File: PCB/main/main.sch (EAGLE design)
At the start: 19 parts, among them T1 2SC1815

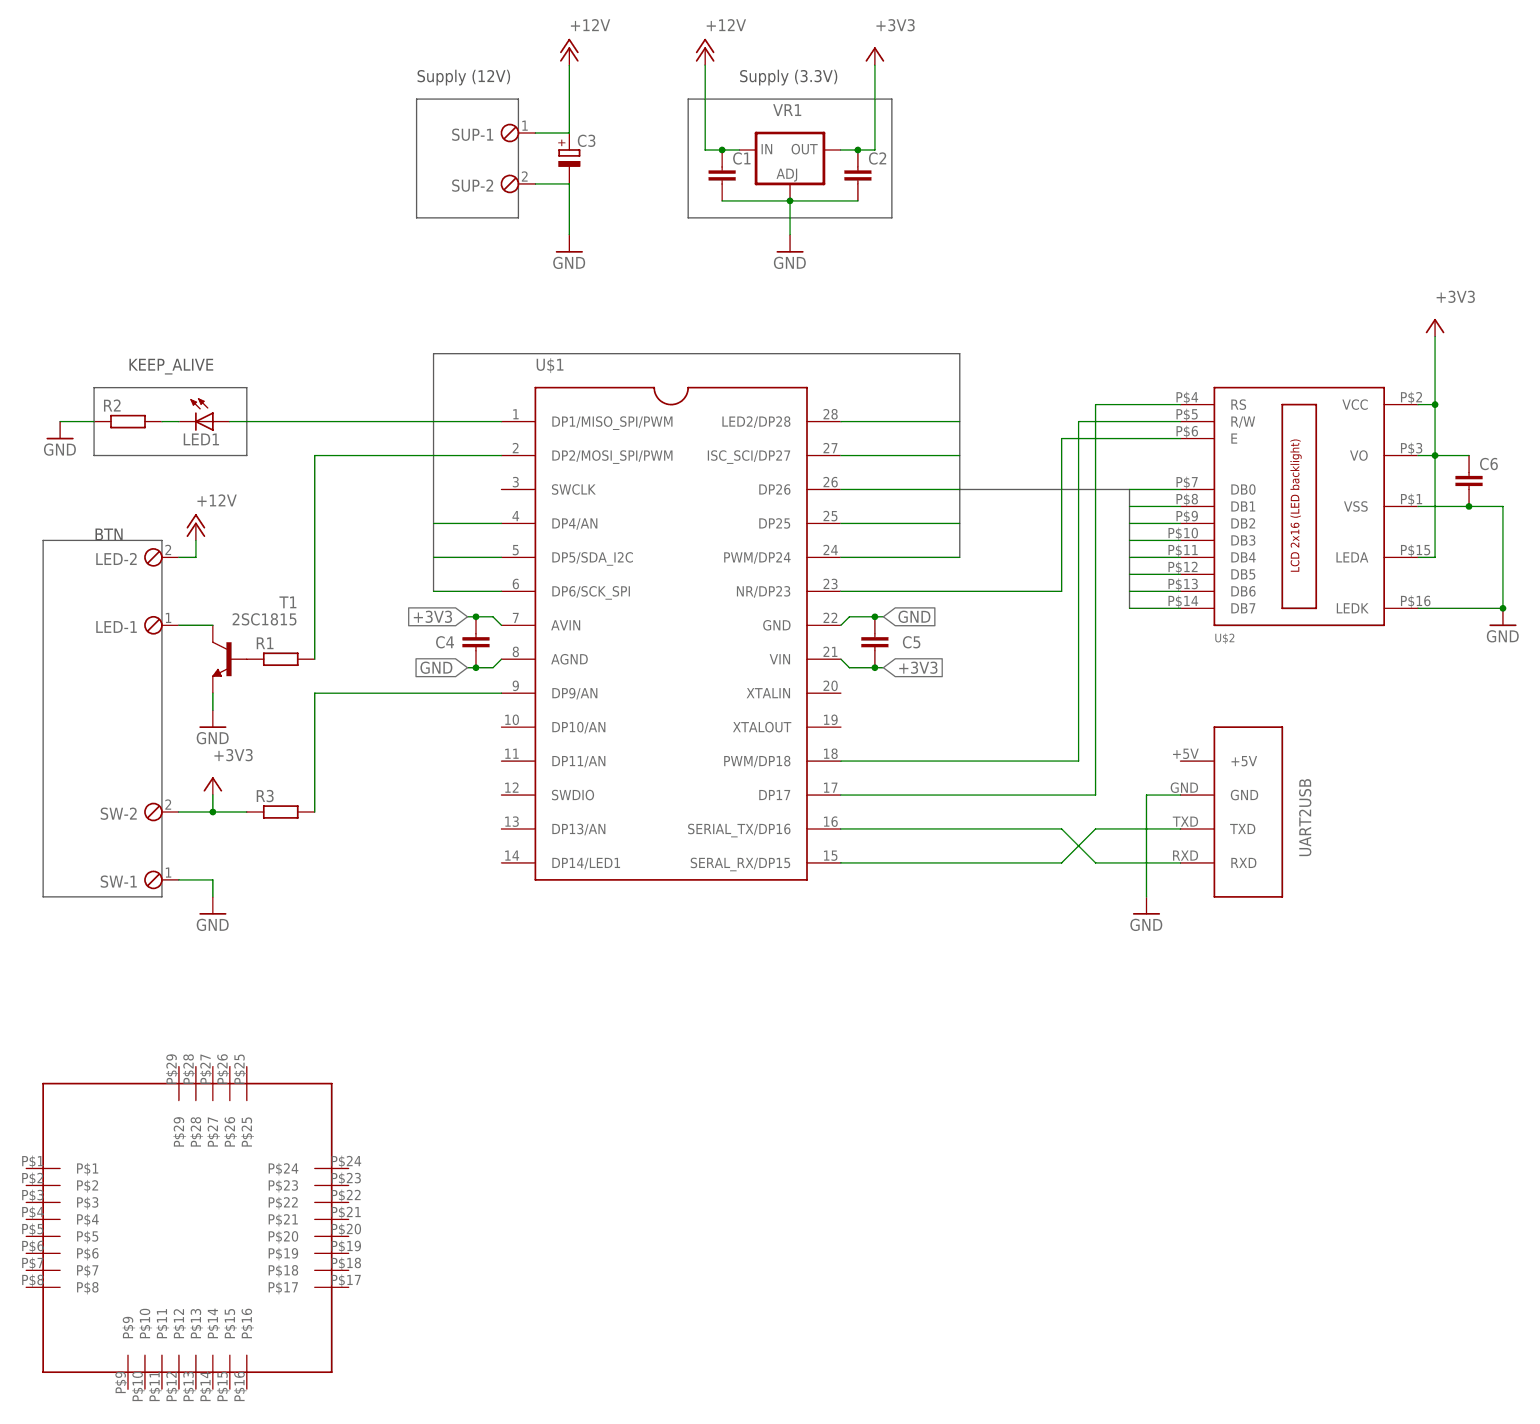
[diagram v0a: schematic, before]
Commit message: PCB: Add DIP con for programing writer like isp writer.
Note that the pin assignment was modified because "reset" and"ISP Enable"
pins are required by "ISP writer" but they were used for LCD.
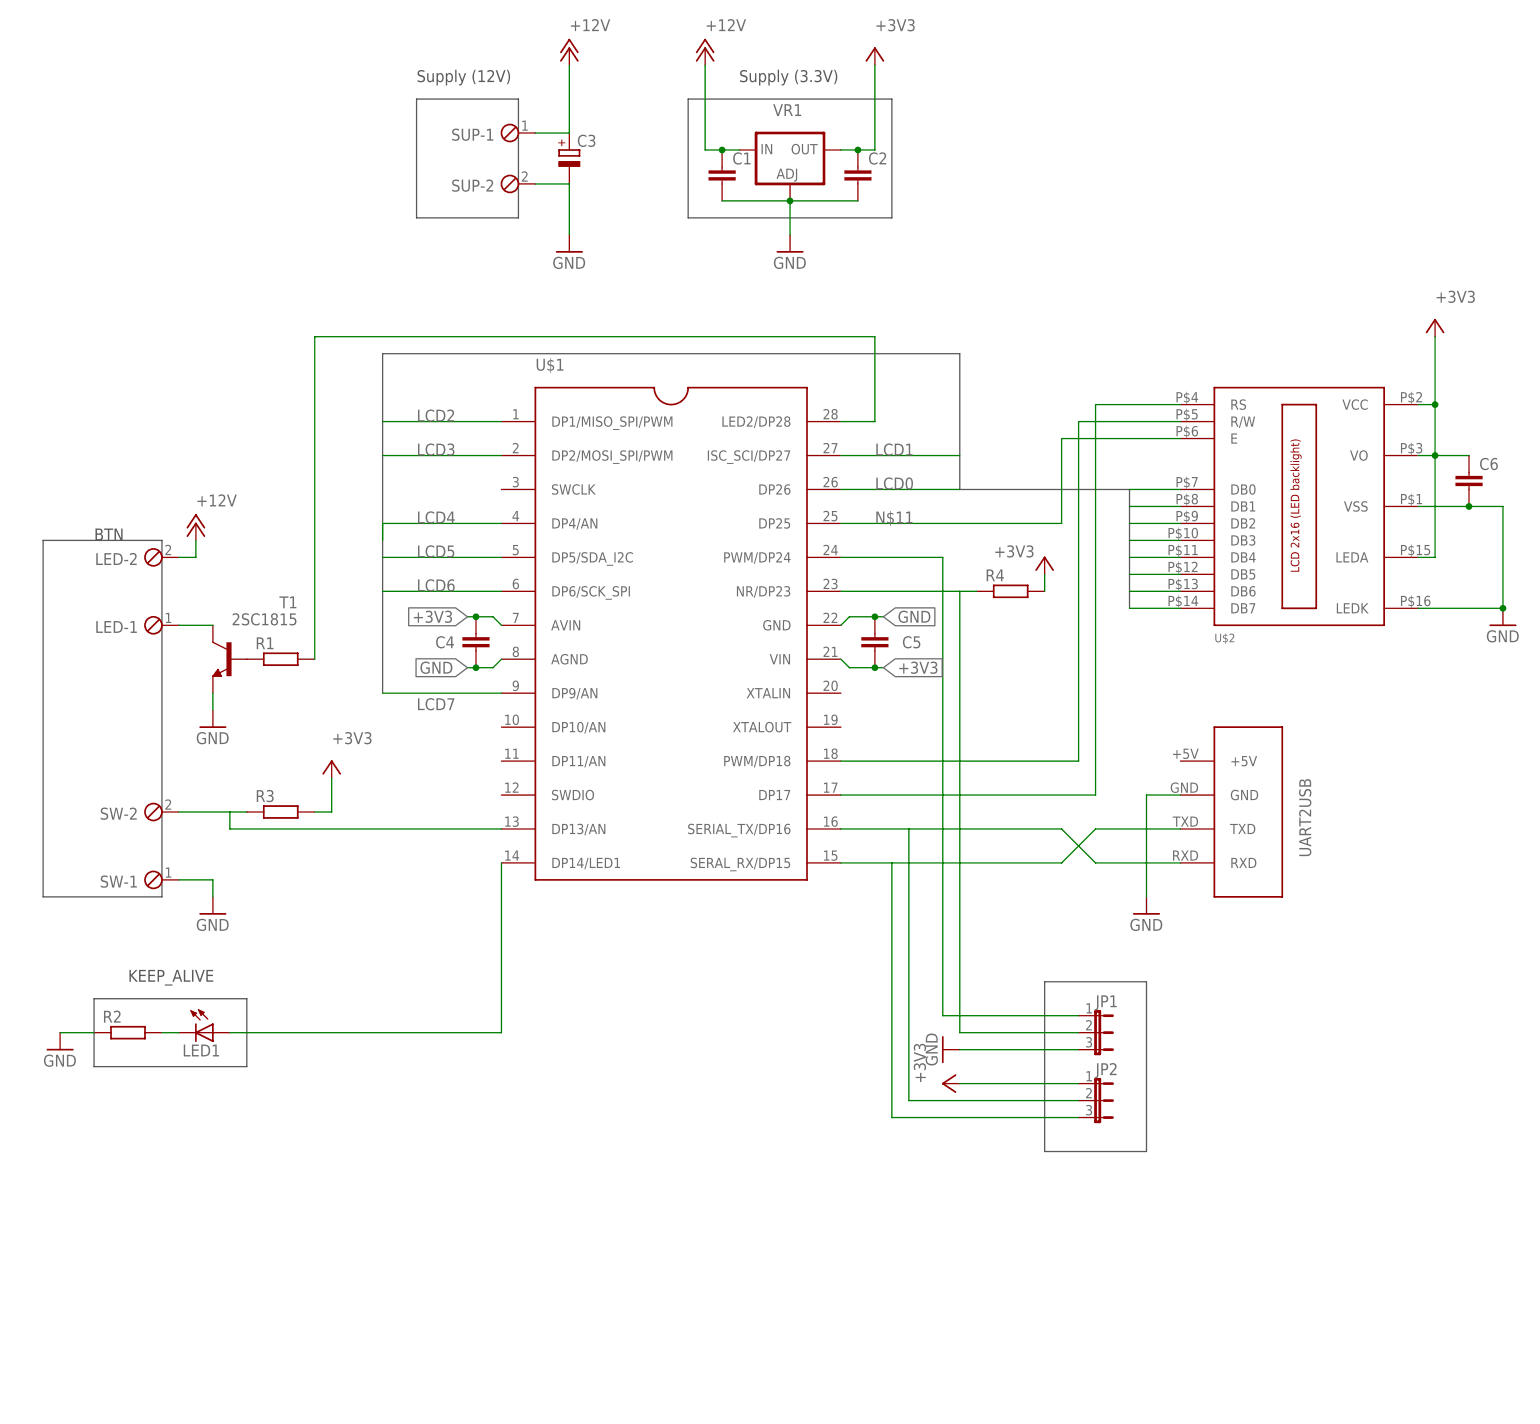
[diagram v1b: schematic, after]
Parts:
- removed U$3: LITE, TWELite:LITE
- added JP1, JP2: (no value), jumper:JP2E
- added R4: (no value), rcl:R-EU_R2012
- R1: device rcl:R-EU_0204/7 -> rcl:R-EU_0207/10
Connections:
- removed net N$13: R3.2, U$1.DP9/AN
- new net N$1: R3.1, SW-2.1, U$1.DP13/AN
- new net N$2: JP2.3, U$1.SERAL_RX/DP15, UART2USB.TXD
- new net N$3: JP2.2, U$1.SERIAL_TX/DP16, UART2USB.RXD
- net +3V3: now also JP2.1, R3.2, R4.2; no longer R3.1, SW-2.1
- net GND: now also JP1.3
- net LCD0: now also U$1.DP26; no longer U$1.PWM/DP24
- net LCD1: now also U$1.ISC_SCI/DP27; no longer U$1.DP25
- net LCD2: now also U$1.DP1/MISO_SPI/PWM; no longer U$1.DP26
- net LCD3: now also U$1.DP2/MOSI_SPI/PWM; no longer U$1.LED2/DP28
- net LCD4: now also U$1.DP4/AN; no longer U$1.ISC_SCI/DP27
- net LCD5: now also U$1.DP5/SDA_I2C; no longer U$1.DP4/AN
- net LCD6: now also U$1.DP6/SCK_SPI; no longer U$1.DP5/SDA_I2C
- net LCD7: now also U$1.DP9/AN; no longer U$1.DP6/SCK_SPI
- net N$10: now also JP1.1, U$1.PWM/DP24; no longer U$1.SERAL_RX/DP15, UART2USB.TXD
- net N$11: now also U$1.DP25; no longer U$1.NR/DP23
- net N$4: now also U$1.DP14/LED1; no longer U$1.DP1/MISO_SPI/PWM
- net N$8: now also U$1.LED2/DP28; no longer U$1.DP2/MOSI_SPI/PWM
- net N$9: now also JP1.2, R4.1, U$1.NR/DP23; no longer U$1.SERIAL_TX/DP16, UART2USB.RXD
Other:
- moved on the sheet: LED1, R2
